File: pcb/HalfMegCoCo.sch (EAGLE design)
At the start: 10 parts, among them IC1 44256, IC2 44256, IC3 44256, IC4 44256, X1 COCO3_RAM_EXPANSION-RP

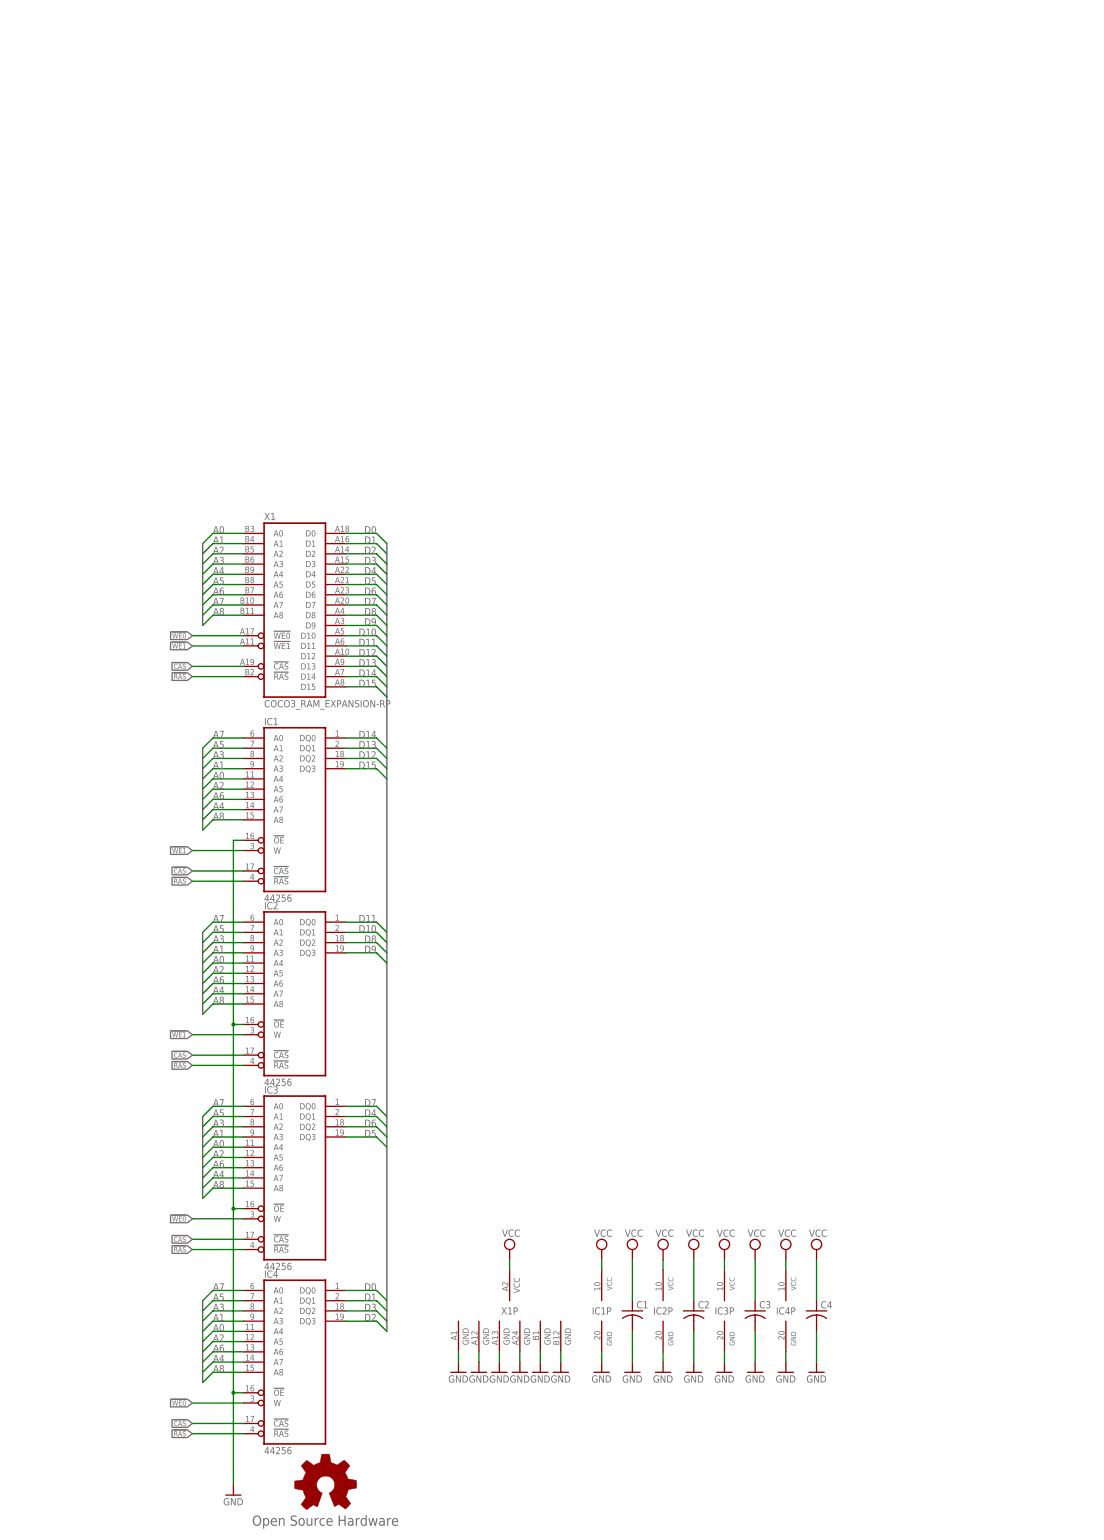
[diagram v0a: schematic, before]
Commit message: SRAM-based version added, DRAM version removed.
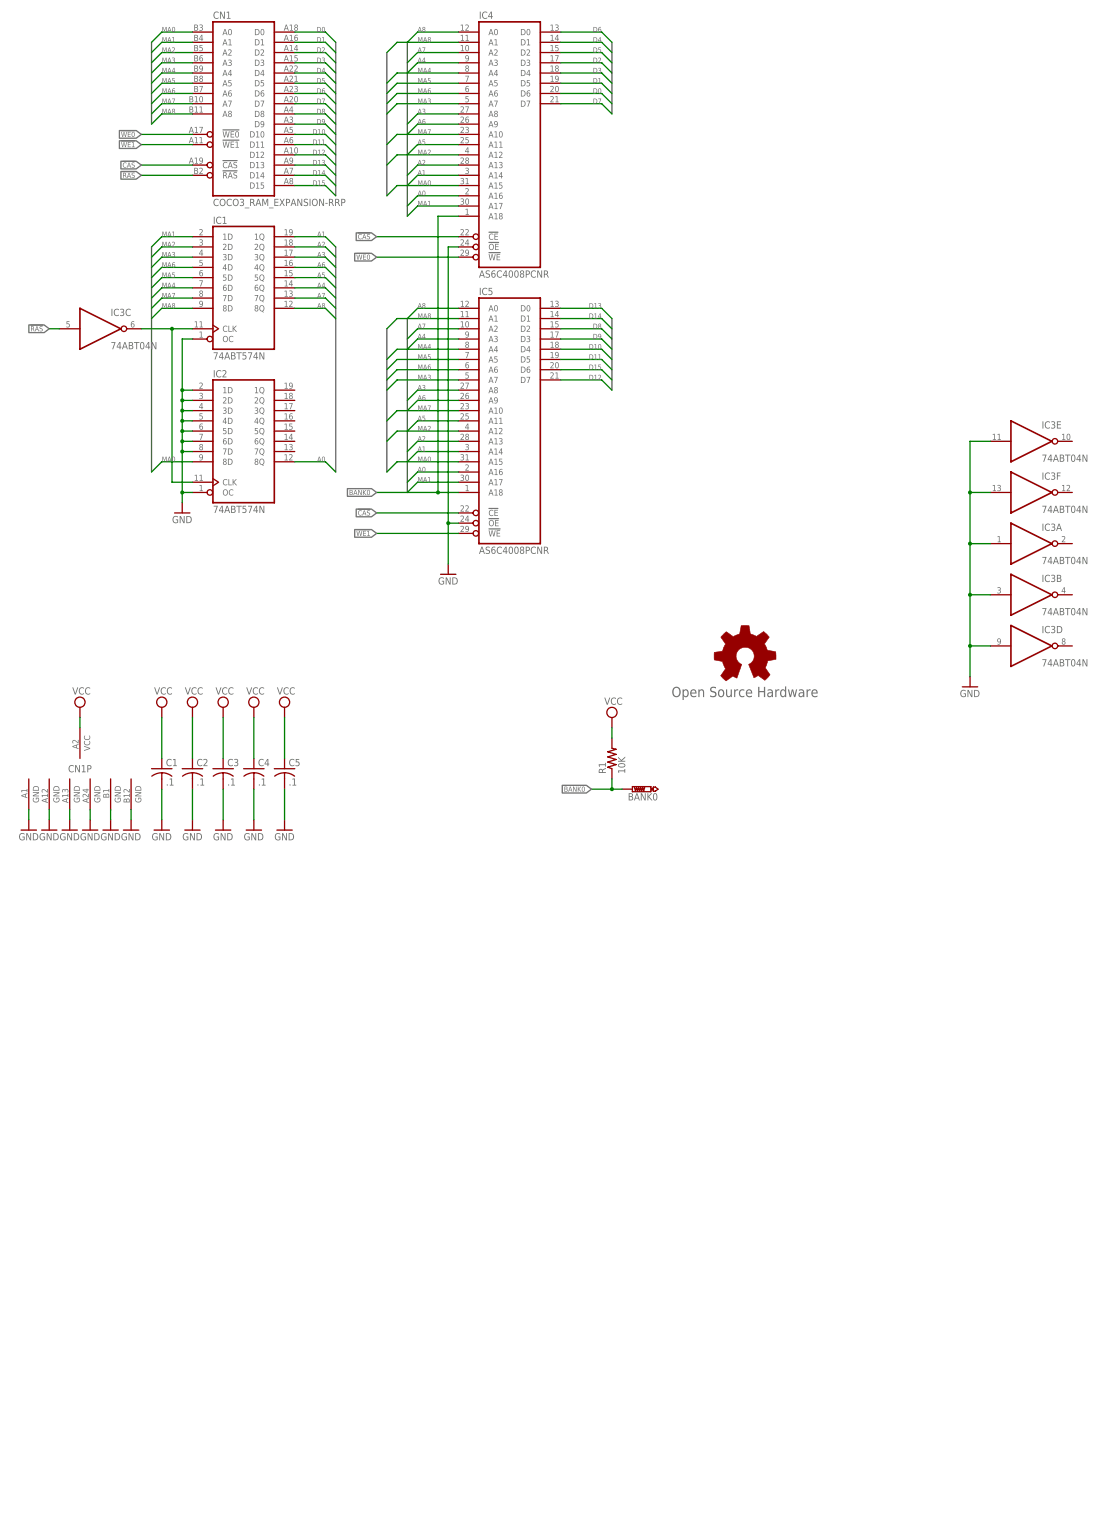
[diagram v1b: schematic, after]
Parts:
- removed X1: COCO3_RAM_EXPANSION-RP, coco:COCO3_RAM_EXPANSION-RP
- added BANK0: PTR1PAD1-13, testpad:PTR1PAD1-13
- added C5: .1, rcl:C-US025-025X050
- added CN1: COCO3_RAM_EXPANSION-RRP, coco:COCO3_RAM_EXPANSION-RRP
- added IC5: AS6C4008PCNR, memory-alliance:AS6C4008PCNR
- added R1: 10K, resistor:R-US_0204/7
- C1, C2, C3, C4: value (none) -> .1; device rcl:C-US050-025X075 -> rcl:C-US025-025X050
- IC1, IC2: value 44256 -> 74ABT574N; device memory-jlb:44256 -> 74xx-us-jlb:74HC574N
- IC3: value 44256 -> 74ABT04N; device memory-jlb:44256 -> 74xx-us-jlb:74ALS04N
- IC4: value 44256 -> AS6C4008PCNR; device memory-jlb:44256 -> memory-alliance:AS6C4008PCNR
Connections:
- new net BANK0: BANK0.TP, IC4A.A18, IC5A.A18, R1.1
- new net MA0: CN1A.A0, IC2A.8D, IC4A.A15, IC5A.A15
- new net MA1: CN1A.A1, IC1A.1D, IC4A.A17, IC5A.A17
- new net MA2: CN1A.A2, IC1A.2D, IC4A.A12, IC5A.A12
- new net MA3: CN1A.A3, IC1A.3D, IC4A.A7, IC5A.A7
- new net MA4: CN1A.A4, IC1A.6D, IC4A.A4, IC5A.A4
- new net MA5: CN1A.A5, IC1A.5D, IC4A.A5, IC5A.A5
- new net MA6: CN1A.A6, IC1A.4D, IC4A.A6, IC5A.A6
- new net MA7: CN1A.A7, IC1A.7D, IC4A.A10, IC5A.A10
- new net MA8: CN1A.A8, IC1A.8D, IC4A.A1, IC5A.A1
- new net N$6: IC1A.CLK, IC2A.CLK, IC3C.O
- net !CAS: now also CN1A.!CAS, IC4A.!CE, IC5A.!CE; no longer IC1A.!CAS, IC2A.!CAS, IC3A.!CAS, IC4A.!CAS, X1A.!CAS
- net !RAS: now also CN1A.!RAS, IC3C.I; no longer IC1A.!RAS, IC2A.!RAS, IC3A.!RAS, IC4A.!RAS, X1A.!RAS
- net !WE0: now also CN1A.!WE0, IC4A.!WE; no longer IC3A.W, IC4A.W, X1A.!WE0
- net !WE1: now also CN1A.!WE1, IC5A.!WE; no longer IC1A.W, IC2A.W, X1A.!WE1
- net A0: now also IC2A.8Q, IC4A.A16, IC5A.A16; no longer IC1A.A4, IC2A.A4, IC3A.A4, IC4A.A4, X1A.A0
- net A1: now also IC1A.1Q, IC4A.A14, IC5A.A14; no longer IC1A.A3, IC2A.A3, IC3A.A3, IC4A.A3, X1A.A1
- net A2: now also IC1A.2Q, IC4A.A13, IC5A.A13; no longer IC1A.A5, IC2A.A5, IC3A.A5, IC4A.A5, X1A.A2
- net A3: now also IC1A.3Q, IC4A.A8, IC5A.A8; no longer IC1A.A2, IC2A.A2, IC3A.A2, IC4A.A2, X1A.A3
- net A4: now also IC1A.6Q, IC4A.A3, IC5A.A3; no longer IC1A.A7, IC2A.A7, IC3A.A7, IC4A.A7, X1A.A4
- net A5: now also IC1A.5Q, IC4A.A11, IC5A.A11; no longer IC1A.A1, IC2A.A1, IC3A.A1, IC4A.A1, X1A.A5
- net A6: now also IC1A.4Q, IC4A.A9, IC5A.A9; no longer IC1A.A6, IC2A.A6, IC3A.A6, IC4A.A6, X1A.A6
- net A7: now also IC1A.7Q, IC4A.A2, IC5A.A2; no longer IC1A.A0, IC2A.A0, IC3A.A0, IC4A.A0, X1A.A7
- net A8: now also IC1A.8Q, IC4A.A0, IC5A.A0; no longer IC1A.A8, IC2A.A8, IC3A.A8, IC4A.A8, X1A.A8
- net D0: now also CN1A.D0, IC4A.D6; no longer IC4A.DQ0, X1A.D0
- net D1: now also CN1A.D1, IC4A.D5; no longer IC4A.DQ1, X1A.D1
- net D10: now also CN1A.D10, IC5A.D4; no longer IC2A.DQ1, X1A.D10
- net D11: now also CN1A.D11, IC5A.D5; no longer IC2A.DQ0, X1A.D11
- net D12: now also CN1A.D12, IC5A.D7; no longer IC1A.DQ2, X1A.D12
- net D13: now also CN1A.D13, IC5A.D0; no longer IC1A.DQ1, X1A.D13
- net D14: now also CN1A.D14, IC5A.D1; no longer IC1A.DQ0, X1A.D14
- net D15: now also CN1A.D15, IC5A.D6; no longer IC1A.DQ3, X1A.D15
- net D2: now also CN1A.D2, IC4A.D3; no longer IC4A.DQ3, X1A.D2
- net D3: now also CN1A.D3, IC4A.D4; no longer IC4A.DQ2, X1A.D3
- net D4: now also CN1A.D4, IC4A.D1; no longer IC3A.DQ1, X1A.D4
- net D5: now also CN1A.D5, IC4A.D2; no longer IC3A.DQ3, X1A.D5
- net D6: now also CN1A.D6, IC4A.D0; no longer IC3A.DQ2, X1A.D6
- net D7: now also CN1A.D7, IC4A.D7; no longer IC3A.DQ0, X1A.D7
- net D8: now also CN1A.D8, IC5A.D2; no longer IC2A.DQ2, X1A.D8
- net D9: now also CN1A.D9, IC5A.D3; no longer IC2A.DQ3, X1A.D9
- net GND: now also C5.2, CN1P.GND, CN1P.GND@1, CN1P.GND@2, CN1P.GND@3, CN1P.GND@4, CN1P.GND@5, IC1A.OC, IC2A.1D, IC2A.2D, IC2A.3D, IC2A.4D, IC2A.5D, IC2A.6D, IC2A.7D, IC2A.OC, IC3A.I, IC3B.I, IC3D.I, IC3E.I, IC3F.I, IC5A.!OE; no longer IC1A.!OE, IC1P.GND, IC2A.!OE, IC2P.GND, IC3A.!OE, IC3P.GND, IC4P.GND, X1P.GND, X1P.GND@1, X1P.GND@2, X1P.GND@3, X1P.GND@4, X1P.GND@5
- net VCC: now also C5.1, CN1P.VCC, R1.2; no longer IC1P.VCC, IC2P.VCC, IC3P.VCC, IC4P.VCC, X1P.VCC
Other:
- moved on the sheet: C1, C2, C3, C4
